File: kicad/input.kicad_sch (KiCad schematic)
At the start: 14 parts, among them U1 NE5532

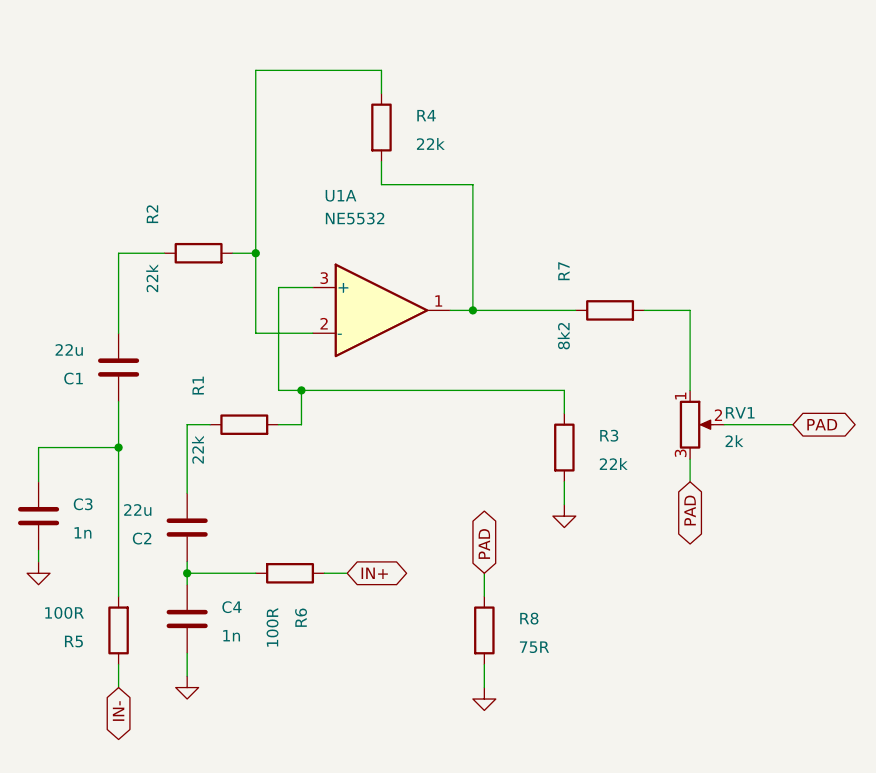
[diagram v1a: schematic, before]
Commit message: Add reorganised schematic to split files.
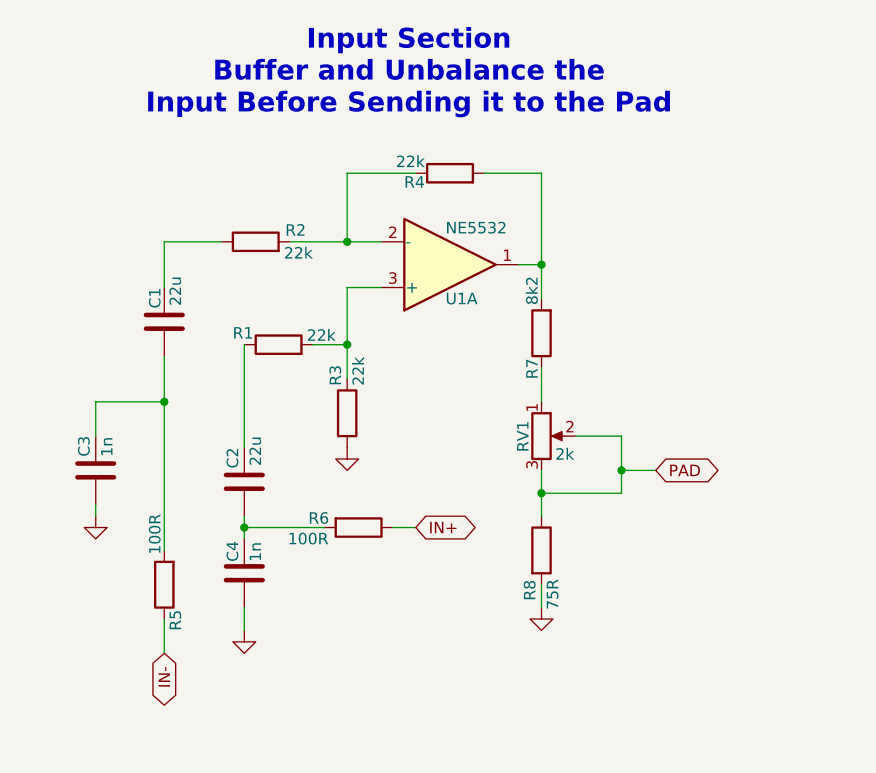
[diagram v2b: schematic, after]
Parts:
- U1: footprint Package_DIP:DIP-8_W7.62mm -> Package_DIP:DIP-8_W7.62mm_Socket
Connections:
- net at R4.2, U1.1: now also R7.2; no longer R7.1
- net at RV1.1: now also R7.1; no longer R7.2
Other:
- note added: "Input Section Buffer and Unbalance the Input Before Sending it to the Pad"
